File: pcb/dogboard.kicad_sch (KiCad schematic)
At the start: 29 parts, among them J1 Barrel_Jack_Switch_Pin3Ring, J2 qtpy1, J3 Conn_01x02_Male, Q1 MMBT3904, Q2 MMBT3904, SW1 SW_Push, U1 LD1117S50TR_SOT223, U2 LM555xN

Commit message: pcb refactor
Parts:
- removed C1, C3, C4: 1uF, Capacitor_SMD:C_1206_3216Metric_Pad1.33x1.80mm_HandSolder, symbol Device:C
- removed C2: 4.7, Capacitor_SMD:C_1206_3216Metric_Pad1.33x1.80mm_HandSolder, symbol Device:C
- removed D1: SB130, Diode_THT:D_DO-41_SOD81_P10.16mm_Horizontal, symbol Diode:SB130
- removed D2: D_Schottky, Diode_SMD:D_1206_3216Metric_Pad1.42x1.75mm_HandSolder, symbol Device:D_Schottky
- removed D3, D4, D5: LED, LED_SMD:LED_1206_3216Metric_Pad1.42x1.75mm_HandSolder, symbol Device:LED
- removed J1: Barrel_Jack_Switch_Pin3Ring, Connector_BarrelJack:BarrelJack_CUI_PJ-102AH_Horizontal, symbol Connector:Barrel_Jack_Switch_Pin3Ring
- removed J2: qtpy1, Module:qtpy1_reverse, symbol Device:qtpy1
- removed J3: Conn_01x02_Male, Connector_JST:JST_PH_S2B-PH-K_1x02_P2.00mm_Horizontal, symbol Connector:Conn_01x02_Male
- removed Q1, Q2: MMBT3904, Package_TO_SOT_SMD:SOT-23, symbol Transistor_BJT:MMBT3904
- removed R1: 47, Resistor_SMD:R_0805_2012Metric_Pad1.20x1.40mm_HandSolder, symbol Device:R
- removed R2, R4, R7: 10k, Resistor_SMD:R_0805_2012Metric_Pad1.20x1.40mm_HandSolder, symbol Device:R
- removed R3: 220, Resistor_SMD:R_0805_2012Metric_Pad1.20x1.40mm_HandSolder, symbol Device:R
- removed R5: 82, Resistor_SMD:R_0805_2012Metric_Pad1.20x1.40mm_HandSolder, symbol Device:R
- removed R6: 150, Resistor_SMD:R_1206_3216Metric_Pad1.30x1.75mm_HandSolder, symbol Device:R
- removed SW1: SW_Push, Button_Switch_THT:SW_PUSH-12mm, symbol Switch:SW_Push
- removed TP3, TP4, TP5, TP6, TP7: TestPoint, TestPoint:TestPoint_Pad_D1.5mm, symbol Connector:TestPoint
- removed U1: LD1117S50TR_SOT223, Package_TO_SOT_SMD:SOT-223-3_TabPin2, symbol Regulator_Linear:LD1117S50TR_SOT223
- removed U2: LM555xN, Package_DIP:DIP-8_W7.62mm, symbol Timer:LM555xN
- added C1, C2: 1uF, _custom:CAP_0805_HandSolder, symbol _custom:CAP_Standard
- added C10, C11, C12, C13, C14, C15, C18, C7, C8: 0.1u, _custom:CAP_0402_HandSolder, symbol _custom:CAP_Standard
- added C4: 0.1u, _custom:CAP_0603_HandSolder, symbol _custom:CAP_Standard
- added C5: 0.1uF, _custom:CAP_0603_HandSolder, symbol _custom:CAP_Standard
- added C6, C9: 1u, _custom:CAP_0603_HandSolder, symbol _custom:CAP_Standard
- added D1: ESD Protection, _custom:tvs_USB2_SOT-723, symbol _custom:TVS_USB_ESD_Protection
- added D6: NeoPxl, _custom:LED_NeoPixel_0606, symbol _custom:LED_NeoPixel
- added J1: USB-C / USB2.0, _custom:USB_C_Receptacle_SMD_GCT, symbol _custom:USB_C_Receptacle_USB2.0_Only
- added R1: 20k, _custom:R_0805_HandSolder, symbol _custom:Resistor_Standard
- added R2, R3: 5.1k, _custom:R_0603_HandSolder, symbol _custom:Resistor_Standard
- added R4: 10k, _custom:R_0805_HandSolder, symbol _custom:Resistor_Standard
- added R6: 1k, _custom:R_0805_HandSolder, symbol _custom:Resistor_Standard
- added R7, R8: 27, _custom:R_0402_HandSolder, symbol _custom:Resistor_Standard
- added REG1: 3.3v Linear, _custom:reg_SMD_SOT-25, symbol _custom:Regulator_SOT-25
- added SW2: BOOT, _custom:button_SMD_PTS810, symbol _custom:SW_Button_Push
- added U1: RP2040, _custom:RP2040_QFN-56, symbol _custom:RP2040
- added U3: 4MB Flash, _custom:flash_SMD_XSON-8_4x4mm, symbol _custom:Flash_Standard
- added Y1: 12 MHz, _custom:XO_Osc_4-SMD_3.2x2.5, symbol _custom:Oscillator_4pin
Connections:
- net GNDREF: now also C1.1, C10.2, C11.2, C12.2, C13.2, C14.2, C15.2, C18.2, C2.1, C4.1, C5.2, C6.2, C7.2, C8.2, C9.2, D1.3 (A), D6.1 (GND), J1.A1 (GND), J1.A12 (GND), J1.B1 (GND), J1.B12 (GND), R1.2, R2.2, R3.2, REG1.2 (GND), SW2.2, U1.19 (TESTEN), U1.57 (GND), U3.4 (GND), Y1.2 (GND)
- new net: R6.1, SW2.1
- new net +1V1: C6.1, C7.1, C8.1, U1.23 (DVDD), U1.45 (VREG_VOUT), U1.50 (DVDD)
- new net +3.3V: C10.1, C11.1, C12.1, C13.1, C14.1, C15.1, C18.1, C2.2, C4.2, C5.1, C9.1, D6.3 (VDD), R4.2, REG1.5 (VO), U1.1 (IOVDD), U1.10 (IOVDD), U1.22 (IOVDD), U1.26 (RUN), U1.33 (IOVDD), U1.42 (IOVDD), U1.43 (ADC_AVDD), U1.44 (VREG_IN), U1.48 (USB_VDD), U1.49 (IOVDD), U3.8 (VCC), Y1.1 (EN), Y1.4 (VDD)
- new net CC1: J1.A5 (CC1), R3.1
- new net CC2: J1.B5 (CC2), R2.1
- new net GNDPWR: J1.S1 (SHIELD), R1.1
- new net GPIO0: U1.2 (GPIO0)
- new net GPIO1: U1.3 (GPIO1)
- new net GPIO10: U1.13 (GPIO10)
- new net GPIO14: U1.17 (GPIO14)
- new net GPIO15: U1.18 (GPIO15)
- new net GPIO16: U1.27 (GPIO16)
- new net GPIO17: U1.28 (GPIO17)
- new net GPIO18: U1.29 (GPIO18)
- new net GPIO19: U1.30 (GPIO19)
- new net GPIO2: U1.4 (GPIO2)
- new net GPIO20: U1.31 (GPIO20)
- new net GPIO21: U1.32 (GPIO21)
- new net GPIO22: U1.34 (GPIO22)
- new net GPIO23: U1.35 (GPIO23)
- new net GPIO24: U1.36 (GPIO24)
- new net GPIO25: U1.37 (GPIO25)
- new net GPIO26: U1.38 (GPIO26_ADC0)
- new net GPIO27: U1.39 (GPIO27_ADC1)
- new net GPIO28: U1.40 (GPIO28_ADC2)
- new net GPIO29: U1.41 (GPIO29_ADC3)
- new net GPIO3: U1.5 (GPIO3)
- new net GPIO4: U1.6 (GPIO4)
- new net GPIO5: U1.7 (GPIO5)
- new net GPIO6: U1.8 (GPIO6)
- new net GPIO7: U1.9 (GPIO7)
- new net GPIO8: U1.11 (GPIO8)
- new net GPIO9: U1.12 (GPIO9)
- new net MEM_IO_{0}: U1.53 (QSPI_SD0), U3.5 (SI/IO_{0})
- new net MEM_IO_{1}: U1.55 (QSPI_SD1), U3.2 (SO/IO_{1})
- new net MEM_IO_{2}: U1.54 (QSPI_SD2), U3.3 (~{WP}/IO_{2})
- new net MEM_IO_{3}: U1.51 (QSPI_SD3), U3.7 (~{RST}/IO_{3})
- new net MEM_SCLK: U1.52 (QSPI_SCLK), U3.6 (SCLK)
- new net NEOSTAT: D6.2 (DIN), U1.14 (GPIO11)
- new net SCL: U1.16 (GPIO13)
- new net SDA: U1.15 (GPIO12)
- new net TR+: R8.2, U1.47 (USB_DP)
- new net TR-: R7.2, U1.46 (USB_DM)
- new net USB_D+: D1.2 (K), J1.A6 (D+), J1.B6 (D+), R8.1
- new net USB_D-: D1.1 (K), J1.A7 (D-), J1.B7 (D-), R7.1
- new net VBUS: C1.2, J1.A4 (VBUS), J1.A9 (VBUS), J1.B4 (VBUS), J1.B9 (VBUS), REG1.1 (VI), REG1.3 (EN)
- new net XIN: U1.20 (XIN), Y1.3 (Out)
- new net ~{BOOT}: R4.1, R6.2, U1.56 (QSPI_SS), U3.1 (~{CS})
- no-connect marks 0 -> 6
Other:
- note added: "Big caps (44+45)"
- note added: "Buttons"
- note added: "Memory"
- note added: "Oscillator"
- note added: "Permanent ON"
- note added: "Power"
- note added: "USB Interface"

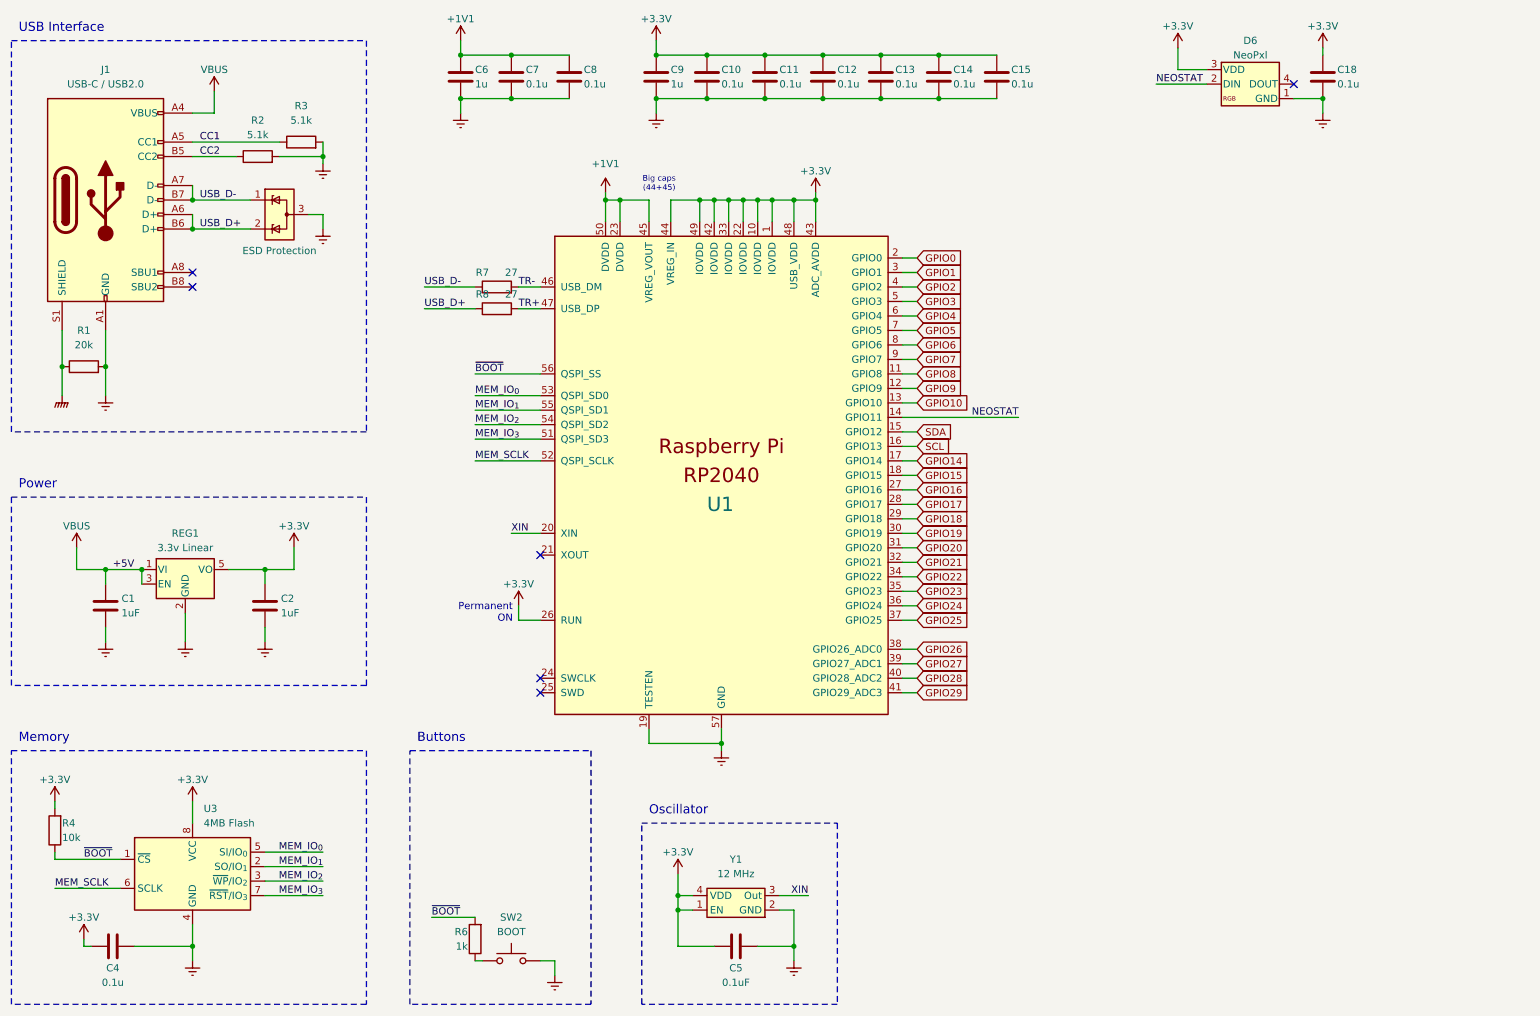
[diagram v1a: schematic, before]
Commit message: rework power regulator
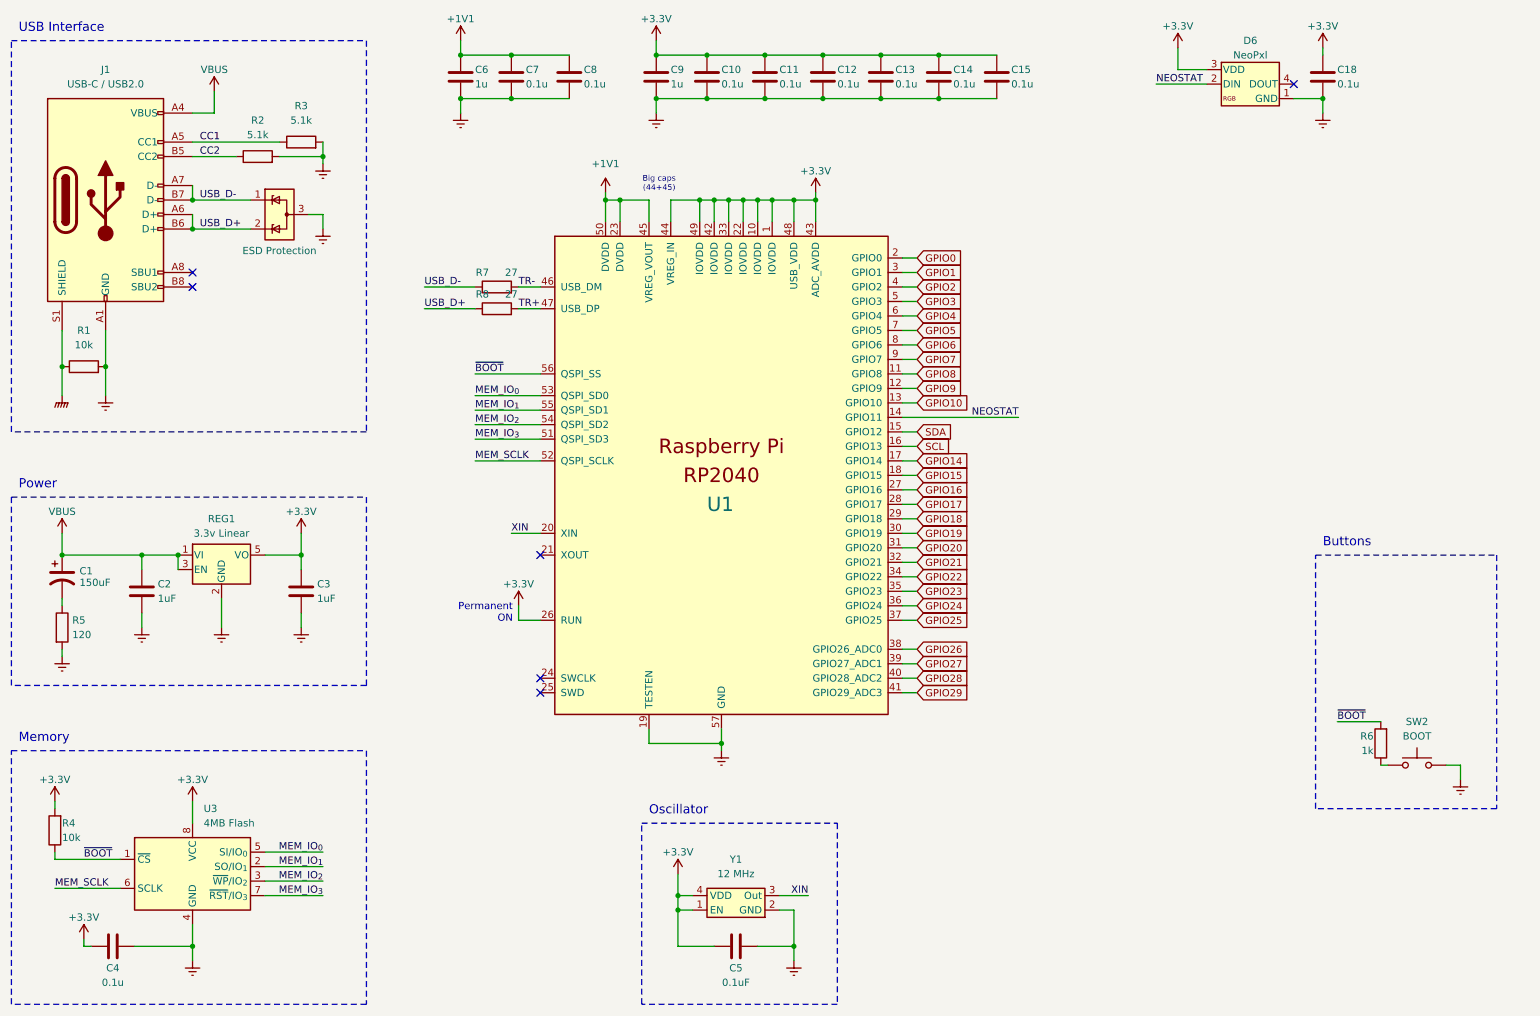
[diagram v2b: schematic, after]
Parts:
- added C1: 150uF, _custom:CAP_Tantalum_2312, symbol _custom:CAP_Tantalum
- added R5: 120, _custom:R_1206_HandSolder, symbol _custom:Resistor_Standard
- R1: value 20k -> 10k; footprint _custom:R_0805_HandSolder -> _custom:R_1206_HandSolder
- SW2: footprint _custom:button_SMD_PTS810 -> _custom:button_metal_smd
- renumbered C1 to C2, C2 to C3
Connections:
- net GNDREF: now also R5.2
- net VBUS: now also C1.1
- new net: C1.2, R5.1
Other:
- moved on the sheet: C2, C3, R6, REG1, SW2

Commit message: PBC rev 2 beta-1
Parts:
- removed C1: 150uF, _custom:CAP_Tantalum_2312, symbol _custom:CAP_Tantalum
- added C1: 10uF, _custom:CAP_1206_NoKeepout, symbol _custom:CAP_Standard
- added C16, C17: 1uF, _custom:CAP_0805_HandSolder, symbol _custom:CAP_Standard
- added D12, D13: MP-LED, _custom:LED_MP-Cathode_1113, symbol _custom:LED_Standard
- added J2: Lights, _custom:conn_1x02_JST_PH_P2.00mm_THT_Horizontal, symbol _custom:Conn_1x02
- added J3: Current Conn, Connector_PinHeader_2.54mm:PinHeader_1x02_P2.54mm_Vertical, symbol Connector:Conn_01x02_Pin
- added R10, R12: 10k, _custom:R_0805_HandSolder, symbol _custom:Resistor_Standard
- added R11: 15k, _custom:R_0805_HandSolder, symbol _custom:Resistor_Standard
- added SW2, SW3: Action, _custom:button_SMD_PTS810, symbol _custom:SW_Button_Push
- added U2: L9110H, _custom:GenericIC_TH-DIP-8, symbol _custom:L9110H_H-Bridge
- added U4: BCR430, _custom:BCR430_CC_LED_Driver, symbol _custom:BCR430_CC_LED_Driver
- C2, C3: value 1uF -> 10uF; footprint _custom:CAP_0805_HandSolder -> _custom:CAP_1206_NoKeepout
- renumbered SW2 to SW1
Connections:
- net +3.3V: now also C17.1, R10.2, R12.2; no longer C3.2
- net GNDREF: now also C16.2, C17.2, R11.2, SW2.2, SW3.2, U4.2 (GND); no longer C2.1, C3.1
- net VBUS: now also C2.1, C3.1, C1.1, C16.1, U2.2 (V_{DD}), U2.3 (V_{DD}), U4.4 (+5v); no longer C2.2
- net GND_RET: now reaches R5.1
- net GND_RET: now also C2.2, C3.2, C1.2
- net GPIO14 renamed SIG_{A}
- net SIG_{A}: now also U2.6 (IN_{A})
- net GPIO15 renamed SIG_{B}
- net SIG_{B}: now also U2.7 (IN_{B})
- net GPIO26 renamed BTN_{ACT}
- net BTN_{ACT}: now also R10.1, SW2.1
- net GPIO27 renamed BTN_{SET}
- net BTN_{SET}: now also R12.1, SW3.1
- new net: R11.1, U4.3 (REXT)
- new net OUT_{A}: J2.1 (Pin_1), J3.1 (Pin_1), U2.1 (OUT_{A})
- new net OUT_{B}: D12.2 (A), D13.2 (A), J2.2 (Pin_2), U2.4 (OUT_{B})
- new net OUT_{C}: D12.1 (K), D13.1 (K), J3.2 (Pin_2)
- new net V_{SS}: U2.5 (V_{SS}), U2.8 (V_{SS}), U4.6 (OUT)
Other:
- added sheet Decor (decor.kicad_sch)
- note added: "Lights Output"
- note added: "Status Ind"
- note added: "Test Circuit"
- moved on the sheet: C18, C5, D6, R5, R6, REG1, SW1, Y1

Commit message: PCB rev 2 beta-2
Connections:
- net OUT_{B}: now also D12.1 (K); no longer D12.2 (A)
- net OUT_{C}: now also D12.2 (A); no longer D12.1 (K)
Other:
- moved on the sheet: D12, D13, J2, J3, R11, U2, U4

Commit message: dogboard-2b3
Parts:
- removed D12, D13: MP-LED, _custom:LED_MP-Cathode_1113, symbol _custom:LED_Standard
- removed J2: Lights, _custom:conn_1x02_JST_PH_P2.00mm_THT_Horizontal, symbol _custom:Conn_1x02
- removed J3: Current Conn, Connector_PinHeader_2.54mm:PinHeader_1x02_P2.54mm_Vertical, symbol Connector:Conn_01x02_Pin
- removed R10, R12: 10k, _custom:R_0805_HandSolder, symbol _custom:Resistor_Standard
- removed R11: 15k, _custom:R_0805_HandSolder, symbol _custom:Resistor_Standard
- removed SW1: BOOT, _custom:button_metal_smd, symbol _custom:SW_Button_Push
- removed U2: L9110H, _custom:GenericIC_TH-DIP-8, symbol _custom:L9110H_H-Bridge
- removed U4: BCR430, _custom:BCR430_CC_LED_Driver, symbol _custom:BCR430_CC_LED_Driver
- added H1, H2, H3, H4: MountingHole, _custom:MountingHole_M2.5, symbol _custom:MountingHole
- added JP1: Boot-Jumper, _custom:Jumper_Open_SMD_3.5mm, symbol _custom:Jumper_Open
- added R10: 10k, _custom:R_Array_4x1206_Convex, symbol _custom:Resistor_Array_4x
- C1: value 10uF -> 150uF; footprint _custom:CAP_1206_NoKeepout -> _custom:CAP_Tantalum_2312
- C2: value 10uF -> 10u
- C3: value 10uF -> 0.1u; footprint _custom:CAP_1206_NoKeepout -> _custom:CAP_0402_HandSolder
- R4, R6: footprint _custom:R_0805_HandSolder -> _custom:R_0603_HandSolder
- U3: value 4MB Flash -> 8MB Flash
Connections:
- net GPIO2 is gone; now on net BTN_{ACT}: U1.4 (GPIO2)
- net GPIO28 is gone; now on net SIG_{B}: U1.40 (GPIO28_ADC2)
- net GPIO5 is gone; now on net BTN_{SET}: U1.7 (GPIO5)
- net +3.3V: now also C3.1, R10.2, R10.4
- net BTN_{ACT}: now also R10.1; no longer U1.38 (GPIO26_ADC0)
- net BTN_{SET}: now also R10.3; no longer U1.39 (GPIO27_ADC1)
- net GNDREF: now also C2.2, C3.2, JP1.2 (B)
- net GND_RET: no longer C2.2, C3.2
- net SIG_{A}: now also U1.39 (GPIO27_ADC1); no longer U1.17 (GPIO14)
- net SIG_{B}: no longer U1.18 (GPIO15)
- net VBUS: no longer C3.1
- net ~{BOOT}: now also R6.1; no longer R6.2
- new net: JP1.1 (A), R6.2
- new net GPIO14: U1.17 (GPIO14)
- new net GPIO15: U1.18 (GPIO15)
- new net GPIO26: U1.38 (GPIO26_ADC0)
- no-connect marks 6 -> 8
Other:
- added sheet Output (output.kicad_sch)
- note added: "Not Required"
- note removed: "Lights Output"
- note removed: "Test Circuit"
- moved on the sheet: C10, C11, C12, C13, C14, C15, C6, C7, C8, C9, SW2, SW3

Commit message: pcb updates
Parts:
- removed unit 1 of R10
- removed unit 2 of R10
- added unit 4 of R10
- C2: value 10u -> 4.7u; footprint _custom:CAP_1206_NoKeepout -> _custom:CAP_0805_NoKeepout
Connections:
- net +3.3V: now also R10.6, R10.8
- net BTN_{ACT}: now also R10.5
- net BTN_{SET}: now also R10.7
- net SCL: now also U1.40 (GPIO28_ADC2); no longer U1.16 (GPIO13)
- net SDA: now also U1.39 (GPIO27_ADC1); no longer U1.15 (GPIO12)
- net SIG_{A}: no longer U1.39 (GPIO27_ADC1)
- net SIG_{B}: no longer U1.40 (GPIO28_ADC2)

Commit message: dogboard-2b4
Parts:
- removed D1: ESD Protection, _custom:tvs_USB2_SOT-723, symbol _custom:TVS_USB_ESD_Protection
- added J4: i2c, _custom:conn_1x04mp_JST_SH_Micro_P1.00mm_Horizontal, symbol _custom:i2c_connector
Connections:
- net GPIO25 is gone; now on net SCL: U1.37 (GPIO25)
- net GPIO26 is gone; now on net SDA: U1.38 (GPIO26_ADC0)
- net GNDREF: now also J4.1 (GND)
- net SCL: no longer U1.40 (GPIO28_ADC2)
- net SDA: no longer U1.39 (GPIO27_ADC1)
- net VBUS: now also J4.2 (+V)
- net GPIO12: now reaches U1.15 (GPIO12)
- net GPIO13: now reaches U1.16 (GPIO13)
- net GPIO14 renamed UART_{RX}
- net UART_{RX}: now also J4.4 (SCL)
- net GPIO15 renamed UART_{TX}
- net UART_{TX}: now also J4.3 (SDA)
- new net GPIO27: U1.39 (GPIO27_ADC1)
- new net GPIO28: U1.40 (GPIO28_ADC2)
- no-connect marks 8 -> 6
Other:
- note added: "Testing"
- moved on the sheet: R10C, R10D, SW2, SW3

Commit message: New board revision
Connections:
- net GPIO12 is gone; now on net UART_{TX}: U1.15 (GPIO12)
- net GPIO13 is gone; now on net UART_{RX}: U1.16 (GPIO13)
- net GPIO24 is gone; now on net SDA: U1.36 (GPIO24)
- net SDA: no longer U1.38 (GPIO26_ADC0)
- net UART_{RX}: no longer U1.17 (GPIO14)
- net UART_{TX}: no longer U1.18 (GPIO15)
- new net GPIO14: U1.17 (GPIO14)
- new net GPIO15: U1.18 (GPIO15)
- new net GPIO26: U1.38 (GPIO26_ADC0)
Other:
- note added: "GPIO 12/13 maps to UART0 See RP2040 DS pg. 13"
- note added: "GPIO 24/25 maps to i^{2}c0 See RP2040 DS pg. 13"
- moved on the sheet: J4, R10C, R10D, SW2, SW3
